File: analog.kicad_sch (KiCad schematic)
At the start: 21 parts, among them Q1 S8550, U2 HX711

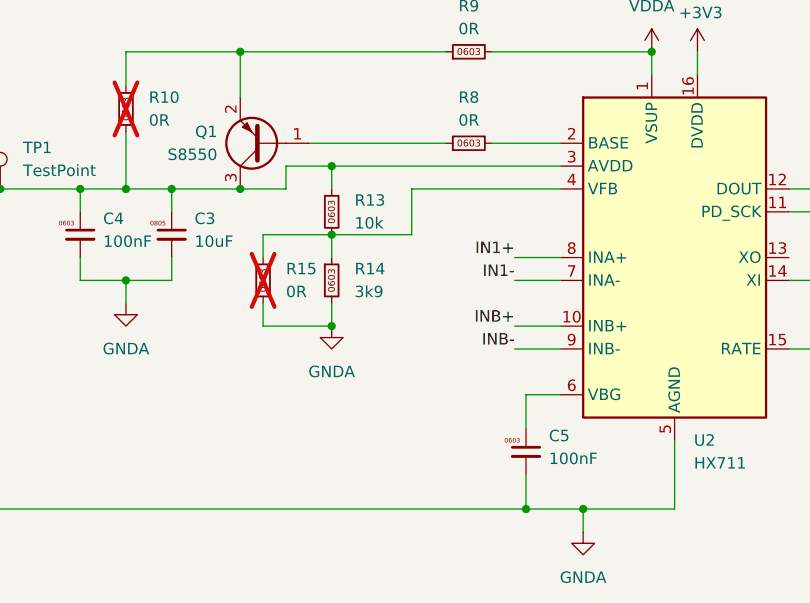
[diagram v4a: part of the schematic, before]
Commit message: wheeww!
Added 3.3v supply from 5V by default.
Added header to access IOs without rpi
Added TP to supply/monitor raw 5V (use without pi)
Adjusted TPs to be on 2.54mm spacing to get headers if desired
Added TVS on EXE+ lines.
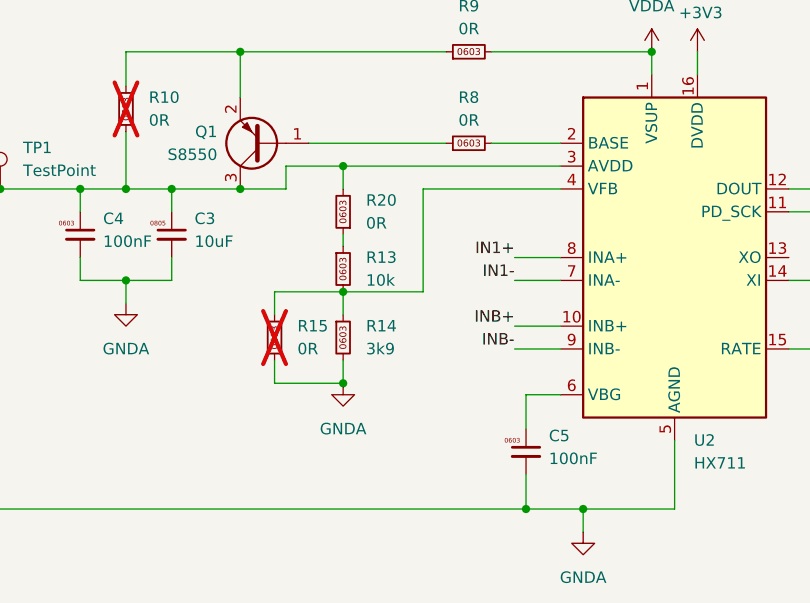
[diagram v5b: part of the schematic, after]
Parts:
- added R20: 0R, Resistor_SMD:R_0603_1608Metric, symbol karl-marel-atomics:KR0603_0R
- TP1: footprint TestPoint:TestPoint_THTPad_1.5x1.5mm_Drill0.7mm -> TestPoint:TestPoint_THTPad_2.0x2.0mm_Drill1.0mm
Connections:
- net EXC+: now also R20.2; no longer R13.1
- new net: R13.1, R20.1
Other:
- moved on the sheet: R13, R14, R15
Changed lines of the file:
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@@
 	)
 	(junction
-		(at 151.13 93.98)
+		(at 152.4 100.33)
 		(diameter 0)
 		(color 0 0 0 0)
@@
 	)
 	(junction
-		(at 186.69 73.66)
+		(at 152.4 86.36)
 		(diameter 0)
 		(color 0 0 0 0)
 	)
 	(junction
-		(at 151.13 104.14)
+		(at 186.69 73.66)
 		(diameter 0)
 		(color 0 0 0 0)
 	)
 	(junction
-		(at 128.27 99.06)
+		(at 152.4 110.49)
 		(diameter 0)
 		(color 0 0 0 0)
 	)
 	(junction
-		(at 140.97 88.9)
+		(at 128.27 99.06)
 		(diameter 0)
 		(color 0 0 0 0)
 	)
 	(junction
-		(at 151.13 86.36)
+		(at 140.97 88.9)
 		(diameter 0)
 		(color 0 0 0 0)
@@
 	(wire
 		(pts
-			(xy 151.13 101.6) (xy 151.13 104.14)
+			(xy 152.4 107.95) (xy 152.4 110.49)
 		)
 		(stroke
@@
 	(wire
 		(pts
-			(xy 160.02 93.98) (xy 151.13 93.98)
+			(xy 161.29 100.33) (xy 152.4 100.33)
 		)
 		(stroke
@@
 	(wire
 		(pts
-			(xy 151.13 93.98) (xy 151.13 96.52)
+			(xy 152.4 100.33) (xy 152.4 102.87)
 		)
 		(stroke
@@
 	(wire
 		(pts
-			(xy 143.51 101.6) (xy 143.51 104.14)
+			(xy 144.78 107.95) (xy 144.78 110.49)
 		)
 		(stroke
@@
 	(wire
 		(pts
+			(xy 152.4 93.98) (xy 152.4 95.25)
+		)
+		(stroke
+			(width 0)
+			(type default)
+		)
+	)
+	(wire
+		(pts
 			(xy 63.5 132.08) (xy 63.5 133.35)
 		)
@@
 	(wire
 		(pts
-			(xy 143.51 104.14) (xy 151.13 104.14)
+			(xy 144.78 110.49) (xy 152.4 110.49)
 		)
 		(stroke
@@
 	(wire
 		(pts
-			(xy 176.53 88.9) (xy 160.02 88.9)
+			(xy 176.53 88.9) (xy 161.29 88.9)
 		)
 		(stroke
@@
 	(wire
 		(pts
-			(xy 143.51 93.98) (xy 151.13 93.98)
+			(xy 144.78 100.33) (xy 152.4 100.33)
 		)
 		(stroke
@@
 	(wire
 		(pts
-			(xy 151.13 86.36) (xy 151.13 88.9)
+			(xy 152.4 86.36) (xy 152.4 88.9)
 		)
 		(stroke
@@
 	(wire
 		(pts
-			(xy 143.51 96.52) (xy 143.51 93.98)
+			(xy 144.78 102.87) (xy 144.78 100.33)
 		)
 		(stroke
@@
 	(wire
 		(pts
-			(xy 160.02 88.9) (xy 160.02 93.98)
+			(xy 161.29 88.9) (xy 161.29 100.33)
 		)
 		(stroke
@@
 	(wire
 		(pts
-			(xy 151.13 86.36) (xy 146.05 86.36)
+			(xy 146.05 86.36) (xy 152.4 86.36)
 		)
 		(stroke
@@
 	(wire
 		(pts
-			(xy 176.53 86.36) (xy 151.13 86.36)
+			(xy 176.53 86.36) (xy 152.4 86.36)
 		)
 		(stroke
@@
 	)
 	(symbol
+		(lib_id "karl-marel-atomics:KR0603_0R")
+		(at 152.4 91.44 180)
+		(unit 1)
+		(exclude_from_sim no)
+		(in_bom yes)
+		(on_board yes)
+		(dnp no)
+		(fields_autoplaced yes)
+		(property "Reference" "R20"
+			(at 154.94 90.1699 0)
+			(effects
+				(font
+					(size 1.27 1.27)
+				)
+				(justify right)
+			)
+		)
+		(property "Value" "0R"
+			(at 154.94 92.7099 0)
+			(effects
+				(font
+					(size 1.27 1.27)
+				)
+				(justify right)
+			)
+		)
+		(property "Footprint" "Resistor_SMD:R_0603_1608Metric"
+			(at 152.4 91.44 0)
+			(effects
+				(font
+					(size 1.27 1.27)
+				)
+				(hide yes)
+			)
+		)
+		(property "Datasheet" "~"
+			(at 152.4 91.44 0)
+			(effects
+				(font
+					(size 1.27 1.27)
+				)
+				(hide yes)
+			)
+		)
+		(property "Description" "Resistor, 0603"
+			(at 152.4 91.44 0)
+			(effects
+				(font
+					(size 1.27 1.27)
+				)
+				(hide yes)
+			)
+		)
+		(property "LCSC Part #" "C21189"
+			(at 152.4 91.44 0)
+			(effects
+				(font
+					(size 1.27 1.27)
+				)
+				(hide yes)
+			)
+		)
+		(property "MPN" "0603WAF0000T5E"
+			(at 152.4 91.44 0)
+			(effects
+				(font
+					(size 1.27 1.27)
+				)
+				(hide yes)
+			)
+		)
+		(property "jlcbasic" "basic"
+			(at 152.4 91.44 90)
+			(effects
+				(font
+					(size 1.27 1.27)
+				)
+				(hide yes)
+			)
+		)
+		(pin "2"
+		)
+		(pin "1"
+		)
+		(instances
+			(project "pi-hat-hx711_r1"
+				(path "/e63e39d7-6ac0-4ffd-8aa3-1841a4541b55/c6a2984f-bea9-4fd5-89c5-8bfdade63ac6"
+					(reference "R20")
+					(unit 1)
+				)
+			)
+		)
+	)
+	(symbol
 		(lib_id "karl-marel-atomics:KC0603_100nF")
 		(at 123.19 93.98 0)
@@
 	(symbol
 		(lib_id "power:GNDA")
-		(at 151.13 104.14 0)
+		(at 152.4 110.49 0)
 		(unit 1)
 		(exclude_from_sim no)
@@
 		(fields_autoplaced yes)
 		(property "Reference" "#PWR017"
-			(at 151.13 110.49 0)
+			(at 152.4 116.84 0)
 			(effects
 				(font
@@
 		)
 		(property "Value" "GNDA"
-			(at 151.13 109.22 0)
+			(at 152.4 115.57 0)
 			(effects
 				(font
@@
 		)
 		(property "Footprint" ""
-			(at 151.13 104.14 0)
+			(at 152.4 110.49 0)
 			(effects
 				(font
@@
 		)
 		(property "Datasheet" ""
-			(at 151.13 104.14 0)
+			(at 152.4 110.49 0)
 			(effects
 				(font
@@
 		)
 		(property "Description" "Power symbol creates a global label with name \"GNDA\" , analog ground"
-			(at 151.13 104.14 0)
+			(at 152.4 110.49 0)
 			(effects
 				(font
@@
 	(symbol
 		(lib_id "karl-marel-atomics:KR0603_10k")
-		(at 151.13 91.44 0)
+		(at 152.4 97.79 0)
 		(unit 1)
 		(exclude_from_sim no)
@@
 		(fields_autoplaced yes)
 		(property "Reference" "R13"
-			(at 153.67 90.1699 0)
+			(at 154.94 96.5199 0)
 			(effects
 				(font
@@
 		)
 		(property "Value" "10k"
-			(at 153.67 92.7099 0)
+			(at 154.94 99.0599 0)
 			(effects
 				(font
@@
 		)
 		(property "Footprint" "Resistor_SMD:R_0603_1608Metric"
-			(at 151.13 91.44 0)
+			(at 152.4 97.79 0)
 			(effects
 				(font
@@
 		)
 		(property "Datasheet" "~"
-			(at 151.13 91.44 0)
+			(at 152.4 97.79 0)
 			(effects
 				(font
@@
 		)
 		(property "Description" "Resistor, 0603"
-			(at 151.13 91.44 0)
+			(at 152.4 97.79 0)
 			(effects
 				(font
@@
 		)
 		(property "MPN" "0603WAF1002T5E"
-			(at 151.13 91.44 0)
+			(at 152.4 97.79 0)
 			(effects
 				(font
@@
 		)
 		(property "LCSC Part #" "C25804"
-			(at 151.13 91.44 0)
+			(at 152.4 97.79 0)
 			(effects
 				(font
@@
 		)
 		(property "jlcbasic" "basic"
-			(at 151.13 91.44 0)
+			(at 152.4 97.79 0)
 			(effects
 				(font
@@
 	(symbol
 		(lib_id "karl-marel-atomics:KR0603_0R")
-		(at 143.51 99.06 180)
+		(at 144.78 105.41 180)
 		(unit 1)
 		(exclude_from_sim no)
@@
 		(fields_autoplaced yes)
 		(property "Reference" "R15"
-			(at 146.05 97.7899 0)
+			(at 147.32 104.1399 0)
 			(effects
 				(font
@@
 		)
 		(property "Value" "0R"
-			(at 146.05 100.3299 0)
+			(at 147.32 106.6799 0)
 			(effects
 				(font
@@
 		)
 		(property "Footprint" "Resistor_SMD:R_0603_1608Metric"
-			(at 143.51 99.06 0)
+			(at 144.78 105.41 0)
 			(effects
 				(font
@@
 		)
 		(property "Datasheet" "~"
-			(at 143.51 99.06 0)
+			(at 144.78 105.41 0)
 			(effects
 				(font
@@
 		)
 		(property "Description" "Resistor, 0603"
-			(at 143.51 99.06 0)
+			(at 144.78 105.41 0)
 			(effects
 				(font
@@
 		)
 		(property "LCSC Part #" "C21189"
-			(at 143.51 99.06 0)
+			(at 144.78 105.41 0)
 			(effects
 				(font
@@
 		)
 		(property "MPN" "0603WAF0000T5E"
-			(at 143.51 99.06 0)
+			(at 144.78 105.41 0)
 			(effects
 				(font
@@
 		)
 		(property "jlcbasic" "basic"
-			(at 143.51 99.06 0)
+			(at 144.78 105.41 0)
 			(effects
 				(font
@@
 			)
 		)
-		(property "Footprint" "TestPoint:TestPoint_THTPad_1.5x1.5mm_Drill0.7mm"
+		(property "Footprint" "TestPoint:TestPoint_THTPad_2.0x2.0mm_Drill1.0mm"
 			(at 119.38 88.9 0)
 			(effects
@@
 	(symbol
 		(lib_id "karl-marel-atomics:KR0603_3k9")
-		(at 151.13 99.06 0)
+		(at 152.4 105.41 0)
 		(unit 1)
 		(exclude_from_sim no)
@@
 		(fields_autoplaced yes)
 		(property "Reference" "R14"
-			(at 153.67 97.7899 0)
+			(at 154.94 104.1399 0)
 			(effects
 				(font
@@
 		)
 		(property "Value" "3k9"
-			(at 153.67 100.3299 0)
+			(at 154.94 106.6799 0)
 			(effects
 				(font
@@
 		)
 		(property "Footprint" "Resistor_SMD:R_0603_1608Metric"
-			(at 151.13 99.06 0)
+			(at 152.4 105.41 0)
 			(effects
 				(font
@@
 		)
 		(property "Datasheet" "~"
-			(at 151.13 99.06 0)
+			(at 152.4 105.41 0)
 			(effects
 				(font
@@
 		)
 		(property "Description" "Resistor, 0603"
-			(at 151.13 99.06 0)
+			(at 152.4 105.41 0)
 			(effects
 				(font
@@
 		)
 		(property "MPN" "0603WAF3901T5E"
-			(at 151.13 99.06 0)
+			(at 152.4 105.41 0)
 			(effects
 				(font
@@
 		)
 		(property "LCSC Part #" "C23018"
-			(at 151.13 99.06 0)
+			(at 152.4 105.41 0)
 			(effects
 				(font
@@
 		)
 		(property "jlcbasic" "basic"
-			(at 151.13 99.06 0)
+			(at 152.4 105.41 0)
 			(effects
 				(font

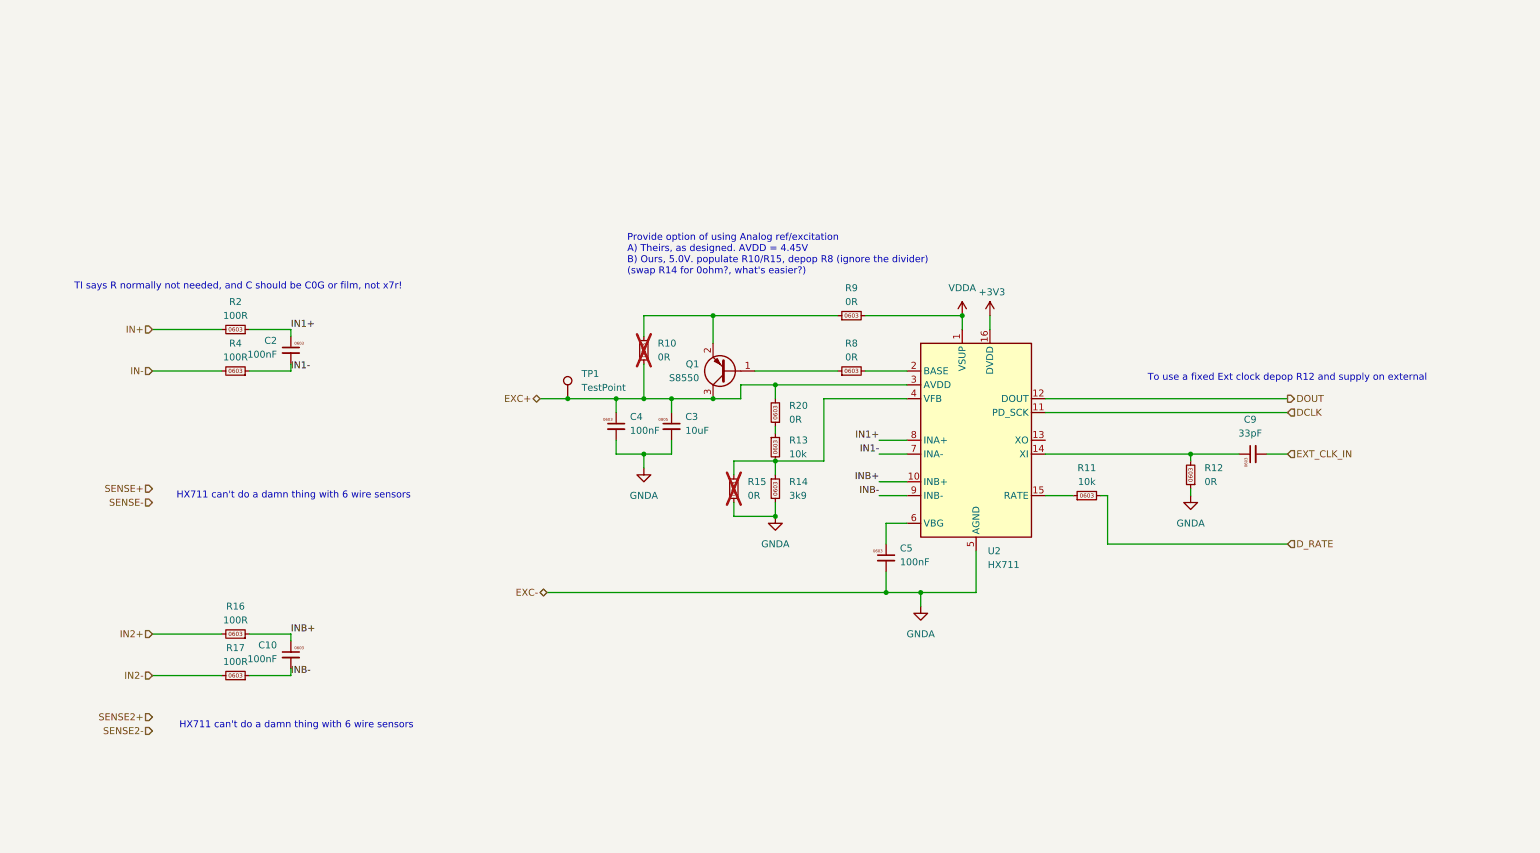
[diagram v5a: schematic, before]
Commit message: erc/drc cleanups
fix lots of off grid stuff that got dragged off in earlier
re-arrangements
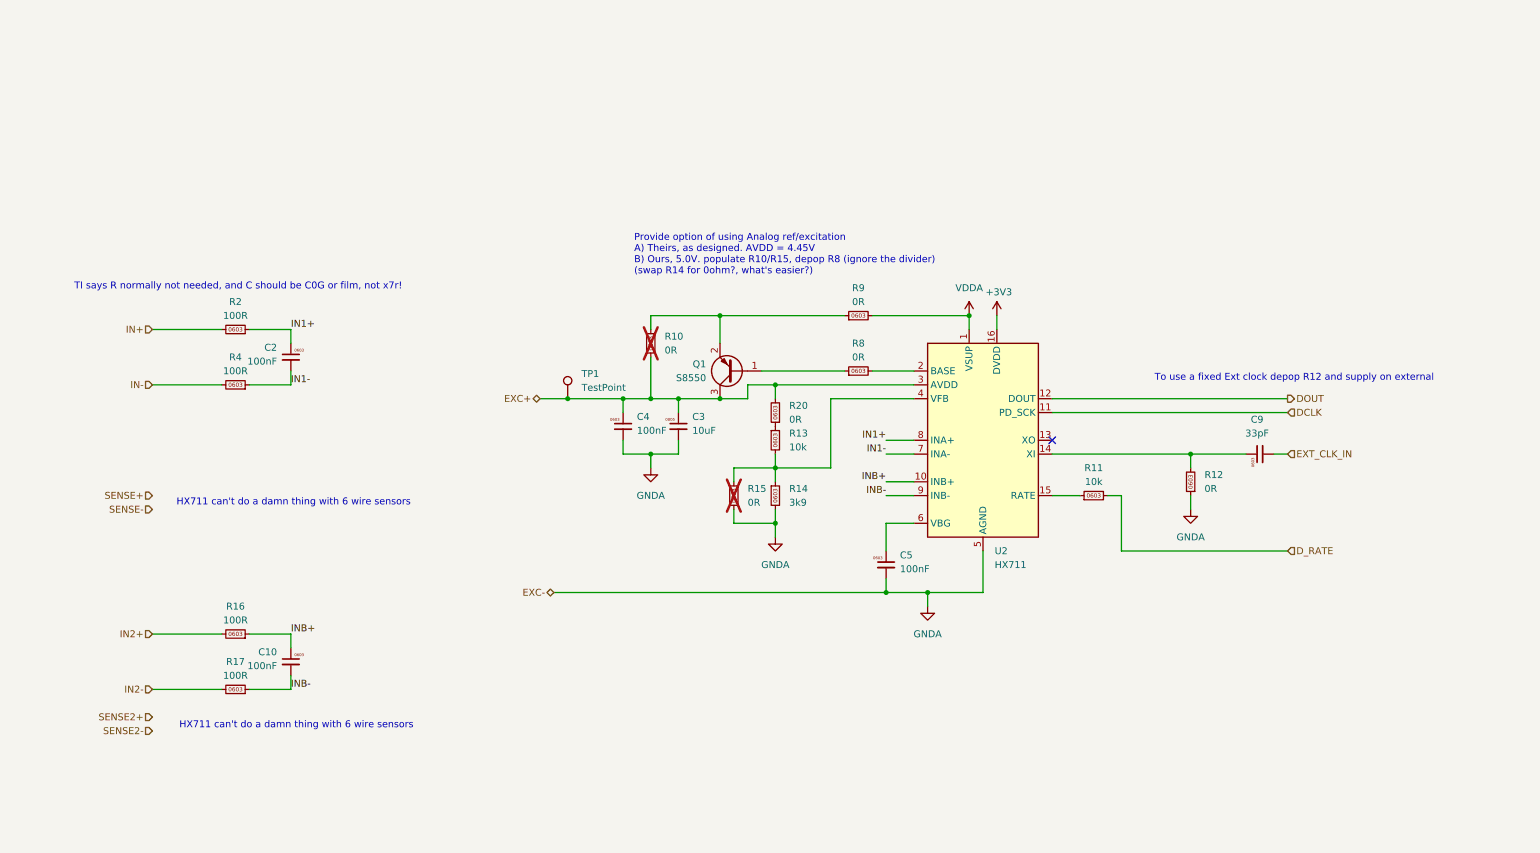
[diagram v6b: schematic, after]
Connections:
- no-connect marks 0 -> 1
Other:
- moved on the sheet: C10, C2, C3, C4, C5, C9, Q1, R10, R11, R12, R13, R14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

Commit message: initial cut.
power and serial interface first cut complete...
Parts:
- removed C3: 10uF, Capacitor_SMD:C_0805_2012Metric, symbol karl-marel-atomics:KC0805_10uF_25V
- removed C4, C5: 100nF, Capacitor_SMD:C_0603_1608Metric, symbol karl-marel-atomics:KC0603_100nF
- removed C9: 33pF, Capacitor_SMD:C_0603_1608Metric, symbol karl-marel-atomics:KC0603_33pF
- removed Q1: S8550, Package_TO_SOT_SMD:SOT-23, symbol Transistor_BJT:BC858
- removed R10, R12, R15, R20, R9: 0R, Resistor_SMD:R_0603_1608Metric, symbol karl-marel-atomics:KR0603_0R
- removed R11, R13: 10k, Resistor_SMD:R_0603_1608Metric, symbol karl-marel-atomics:KR0603_10k
- removed R14: 3k9, Resistor_SMD:R_0603_1608Metric, symbol karl-marel-atomics:KR0603_3k9
- removed U2: HX711, Package_SO:SOIC-16_3.9x9.9mm_P1.27mm, symbol Analog_ADC:HX711
- added C18: 330nF, Capacitor_SMD:C_0603_1608Metric, symbol karl-marel-atomics:KC0603_330nF
- added C3: 100nF, Capacitor_SMD:C_0603_1608Metric, symbol karl-marel-atomics:KC0603_100nF
- added C4: 1uF, Capacitor_SMD:C_0603_1608Metric, symbol karl-marel-atomics:KC0603_1uF
- added TP6: TestPoint, TestPoint:TestPoint_THTPad_2.0x2.0mm_Drill1.0mm, symbol Connector:TestPoint
- added U2: ADS124S08, Package_QFP:TQFP-32_5x5mm_P0.5mm, symbol karl-marel-atomics:ADS124S08IPBSR
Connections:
- net +3V3: now also C3.1, U2.15 (IOVDD), U2.16 (DVDD)
- net GNDA: now also C18.2, U2.27 (AVSS), U2.28 (AVSS_SW)
- net VDDA: now also C18.1, U2.26 (AVDD)
- net GND: now reaches R8.1
- net GND: now also C3.2, C4.2, U2.14 (DGND), U2.24 (REFCOM)
- net EXT_CLK: now reaches R8.2
- net EXT_CLK: now also U2.17 (CLK)
- new net: C4.1, U2.23 (REFOUT)
- new net ADC_START: U2.8 (START/SYNC)
- new net EXC2+: TP6.1
- new net SPI_CLK: U2.11 (SCLK)
- new net SPI_CS: U2.9 (~{CS})
- new net SPI_MISO: U2.12 (DOUT/~{DRDY})
- new net SPI_MOSI: U2.10 (DIN)
- new net ~{ADC_READY}: U2.13 (~{DRDY})
- new net ~{ADC_RST}: U2.18 (~{RESET})
- no-connect marks 1 -> 0
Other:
- note added: "Remove to use ext-clock"
- note added: "TI sez: 47R on allll serial lines, but... yolo"
- note added: "vdda is 5v"
- note removed: "HX711 can't do a damn thing with 6 wire sensors"
- note removed: "Provide option of using Analog ref/excitation A) Theirs, as designed. AVDD = 4.45V B) Ours, 5.0V. populate R10/R15, depop R8 (ignore the divider) (swap R14 for 0ohm?, what's easier?)"
- note removed: "To use a fixed Ext clock depop R12 and supply on external"
- moved on the sheet: TP1

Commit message: blocking out...
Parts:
- removed C18: 330nF, Capacitor_SMD:C_0603_1608Metric, symbol karl-marel-atomics:KC0603_330nF
- removed C2: 100nF, Capacitor_SMD:C_0603_1608Metric, symbol karl-marel-atomics:KC0603_100nF
- removed R16, R17, R2, R4: 100R, Resistor_SMD:R_0603_1608Metric, symbol karl-marel-atomics:KR0603_100R
- removed TP1, TP6: TestPoint, TestPoint:TestPoint_THTPad_2.0x2.0mm_Drill1.0mm, symbol Connector:TestPoint
- added C17: 10nF, Capacitor_SMD:C_0603_1608Metric, symbol karl-marel-atomics:KC0603_10nF_C0G
- added C5, C9: 220nF, Capacitor_SMD:C_0603_1608Metric, symbol karl-marel-atomics:KC0603_220nF
- added R10, R9: 1k, Resistor_SMD:R_0603_1608Metric, symbol karl-marel-atomics:KR0603_1k
- added R2, R4: 10k, Resistor_SMD:R_0603_1608Metric, symbol karl-marel-atomics:KR0603_10k
- added unit 1 of U2
- added unit 2 of U2
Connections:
- net ADC_START: now also U2.8 (START/SYNC); no longer U2.8 (START/SYNC)
- net EXT_CLK: now also U2.17 (CLK); no longer U2.17 (CLK)
- net GNDA: now also C5.2, C9.2
- net IN1+: now also R2.1
- net IN1-: now also R4.1
- net IN2+: now also R9.1
- net IN2-: now also R10.1
- net INB+: now also R9.2, U2.7 (AIN0)
- net INB-: now also R10.2, U2.6 (AIN1)
- net SENSE2+: now also U2.32 (REFP1/AIN6)
- net SENSE2-: now also U2.31 (REFN1/AIN7)
- net SPI_CLK: now also U2.11 (SCLK); no longer U2.11 (SCLK)
- net SPI_CS: now also U2.9 (~{CS}); no longer U2.9 (~{CS})
- net SPI_MISO: now also U2.12 (DOUT/~{DRDY}); no longer U2.12 (DOUT/~{DRDY})
- net SPI_MOSI: now also U2.10 (DIN); no longer U2.10 (DIN)
- net VDDA: now also C5.1, C9.1
- net ~{ADC_READY}: now also U2.13 (~{DRDY}); no longer U2.13 (~{DRDY})
- net ~{ADC_RST}: now also U2.18 (~{RESET}); no longer U2.18 (~{RESET})
- new net INA+: C17.1, R2.2, U2.5 (AIN2)
- new net INA-: C17.2, R4.2, U2.4 (AIN3)
- new net SENSE1+: U2.30 (REFP0)
- new net SENSE1-: U2.29 (REFN0)
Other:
- note added: "Remember, you're _NOT_ making an eval board for the ADC! DO NOT TRY AND DO EVERYTHING POSSIBLE!"
- note added: "So. 4ksps ADC. set a 3db poitn of 3180. that's fine. Use NP0 on one channel, 10nF to keep cost/size down, use X7r on another channel pair, see if we can see the difference?"
